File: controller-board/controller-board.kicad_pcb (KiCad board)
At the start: 2 copper layers, 130 x 95 mm, 96 parts, among them J1 Conn_01x02, J2 Conn_01x02, J3 Conn_01x02, J4 Conn_01x02, J5 Conn_01x03, J6 Conn_01x02, J7 Conn_01x02, Q1 PMV45EN2, Q3 RQ3E120ATTB, U1 CAT4201, U2 PocketBeagle, U3 LTC3624, U4 CAT4201, U5 CAT4201, U6 CAT4201, U7 MCP4728, U8 ADC108S022

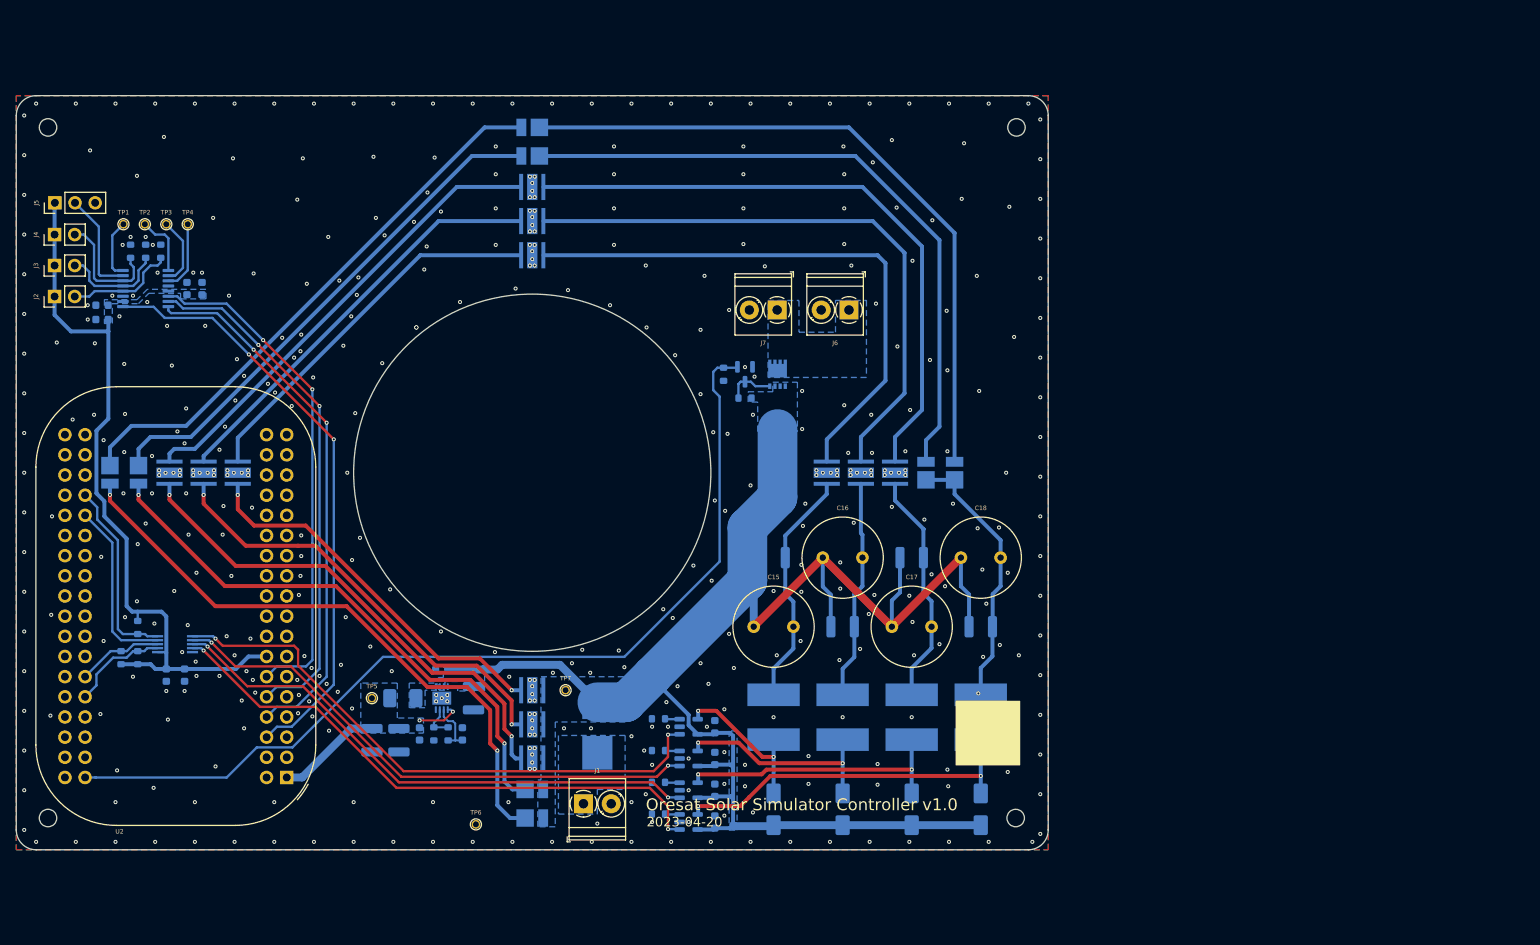
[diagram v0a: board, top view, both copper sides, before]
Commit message: Updated mounting holes and fixed some errors
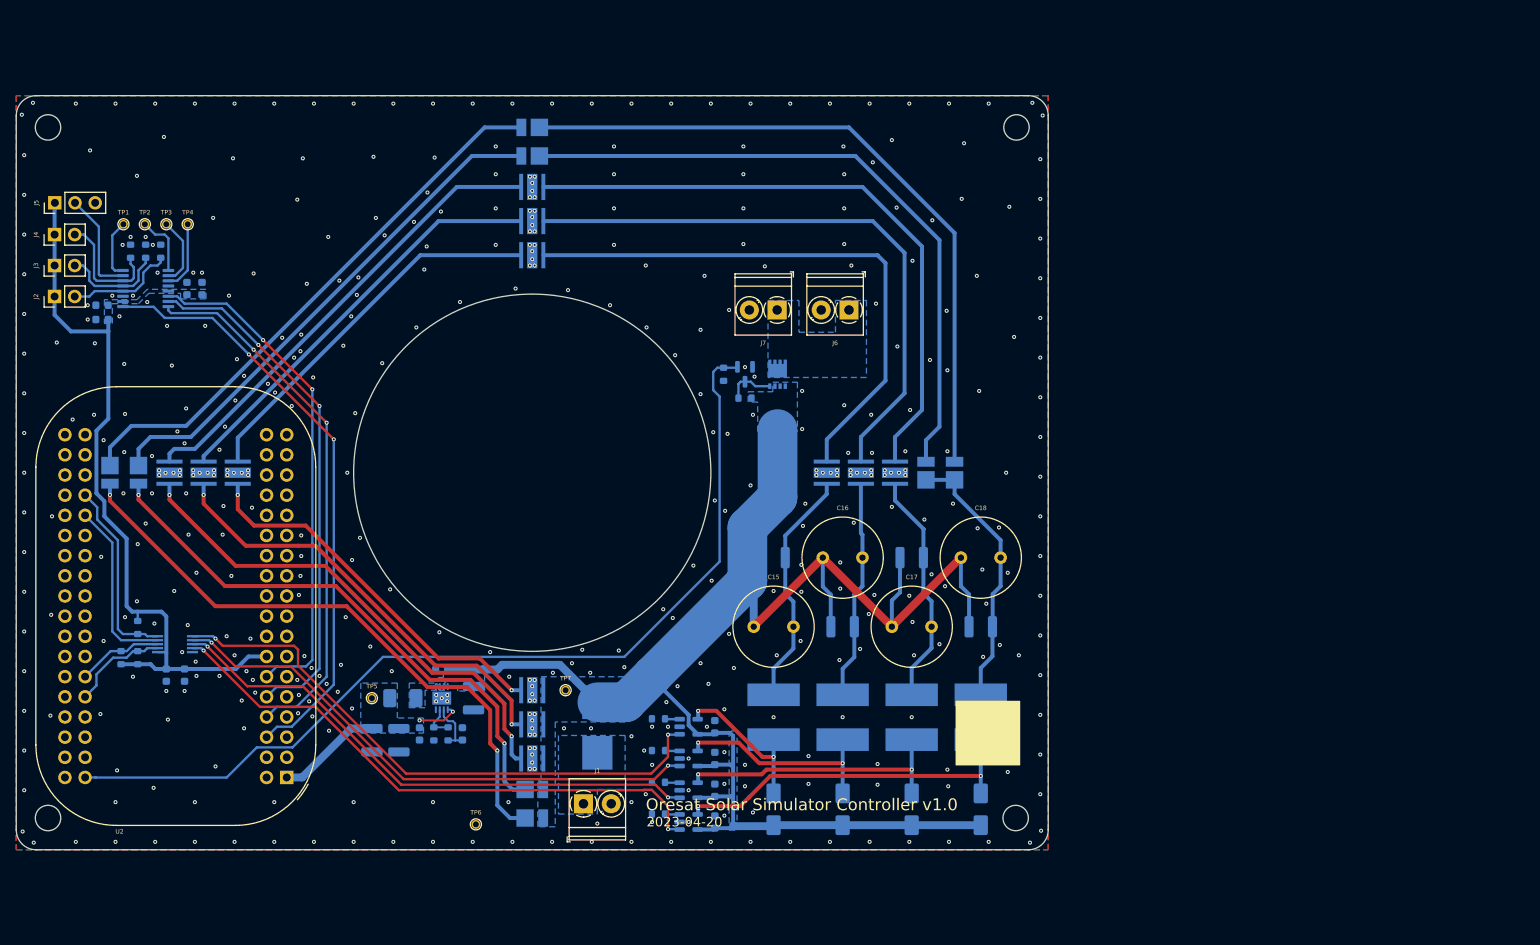
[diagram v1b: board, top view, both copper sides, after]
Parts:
- REF** (x4): value MountingHole_2.2mm_M2 -> MountingHole_3.2mm_M3; footprint MountingHole:MountingHole_2.2mm_M2 -> MountingHole:MountingHole_3.2mm_M3
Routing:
- net GND: vias 454 -> 452

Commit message: Updated main PCB. Added lots of LEDs and moved things around. Fixed some issues.
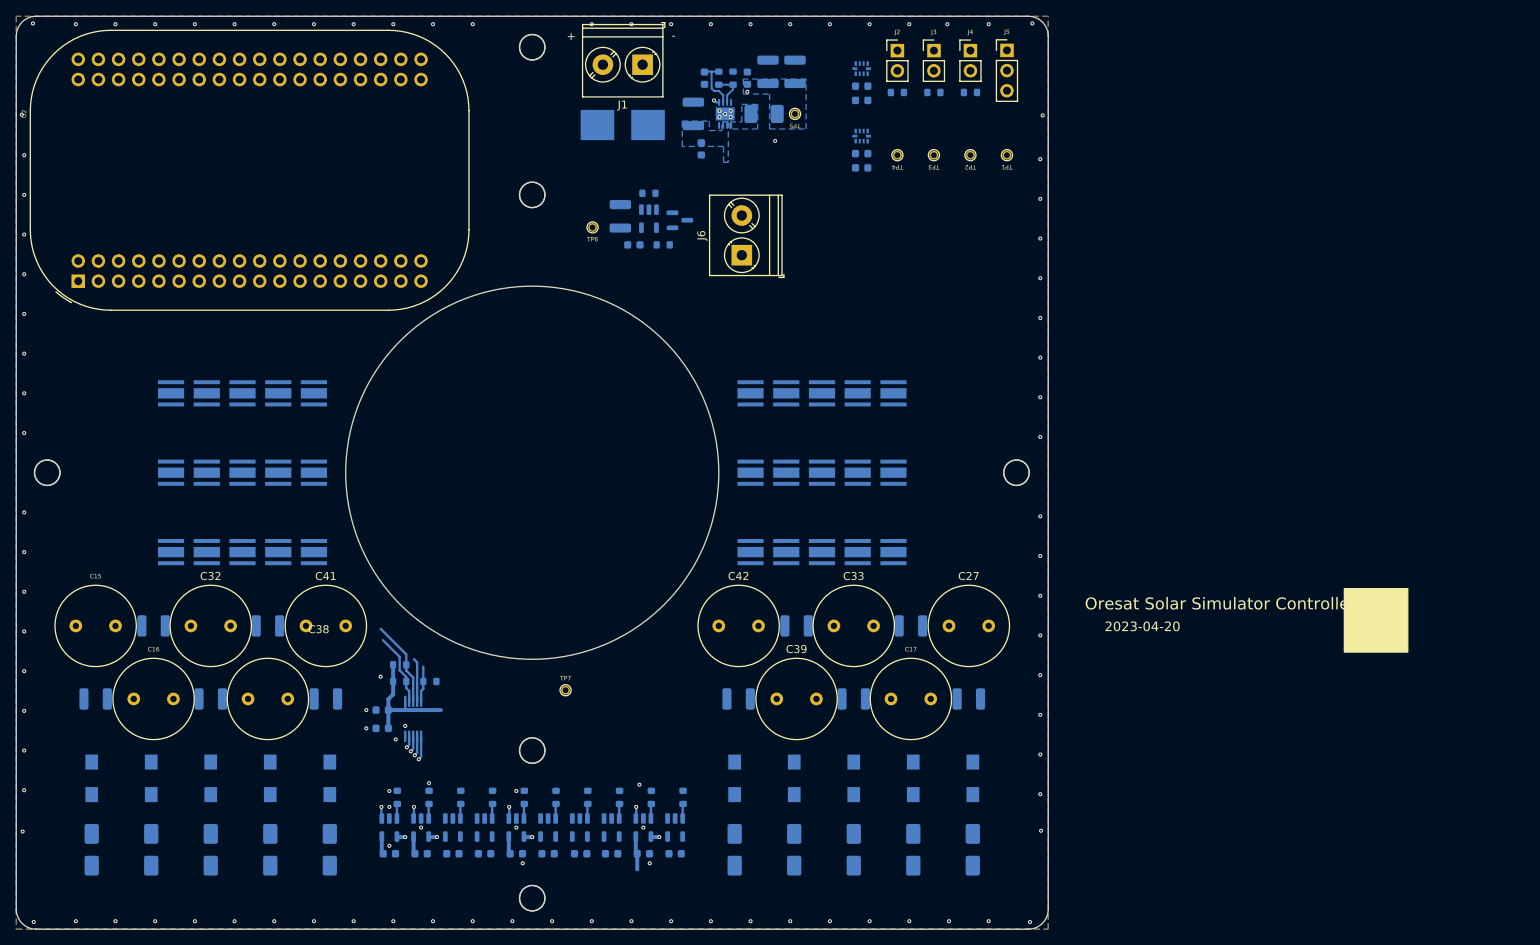
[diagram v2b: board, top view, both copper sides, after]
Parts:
- removed D24: 153283367A212, LED_SMD:LED_PLCC_2835
- removed J7: Conn_01x02, TerminalBlock_Phoenix:TerminalBlock_Phoenix_PT-1,5-2-3.5-H_1x02_P3.50mm_Horizontal
- removed Q3: RQ3E120ATTB, Package_SON:Diodes_PowerDI3333-8
- added C25: 4.7u, Capacitor_SMD:C_0603_1608Metric, B.Cu at (163.0, 150.5)
- added C26: 22u, Capacitor_SMD:C_1210_3225Metric, B.Cu at (200.0, 131.0)
- added C27: NP, Capacitor_THT:C_Radial_D10.0mm_H16.0mm_P5.00mm, F.Cu at (197.5, 121.8)
- added C28: 4.7u, Capacitor_SMD:C_0603_1608Metric, B.Cu at (135.0, 150.5)
- added C29: 4.7u, Capacitor_SMD:C_0603_1608Metric, B.Cu at (155.0, 150.5)
- added C30: 22u, Capacitor_SMD:C_1210_3225Metric, B.Cu at (104.5, 131.0)
- added C31: 22u, Capacitor_SMD:C_1210_3225Metric, B.Cu at (185.5, 131.0)
- added C32: NP, Capacitor_THT:C_Radial_D10.0mm_H16.0mm_P5.00mm, F.Cu at (102.0, 121.8)
- added C33: NP, Capacitor_THT:C_Radial_D10.0mm_H16.0mm_P5.00mm, F.Cu at (183.0, 121.8)
- added C34: 4.7u, Capacitor_SMD:C_0603_1608Metric, B.Cu at (139.0, 150.5)
- added C35: 4.7u, Capacitor_SMD:C_0603_1608Metric, B.Cu at (151.1, 150.5)
- added C36: 22u, Capacitor_SMD:C_1210_3225Metric, B.Cu at (111.7, 121.8)
- added C37: 22u, Capacitor_SMD:C_1210_3225Metric, B.Cu at (178.3, 121.8)
- added C38: NP, Capacitor_THT:C_Radial_D10.0mm_H16.0mm_P5.00mm, F.Cu at (109.2, 131.0)
- added C39: NP, Capacitor_THT:C_Radial_D10.0mm_H16.0mm_P5.00mm, F.Cu at (175.8, 131.0)
- added C40: 22u, Capacitor_SMD:C_1210_3225Metric, B.Cu at (171.0, 131.0)
- added C41: NP, Capacitor_THT:C_Radial_D10.0mm_H16.0mm_P5.00mm, F.Cu at (116.5, 121.8)
- added C42: NP, Capacitor_THT:C_Radial_D10.0mm_H16.0mm_P5.00mm, F.Cu at (168.5, 121.8)
- added C43: 22u, Capacitor_SMD:C_1210_3225Metric, B.Cu at (156.1, 70.2)
- added C44: 1u, Capacitor_SMD:C_0603_1608Metric, B.Cu at (157.8, 73.8)
- added D25: XPEBRD-L1-0000-00501, LED_SMD:LED_Cree-XP, B.Cu at (190.5, 92.5)
- added D26: XPEBRD-L1-0000-00501, LED_SMD:LED_Cree-XP, B.Cu at (190.5, 112.5)
- added D27: XPEBRD-L1-0000-00501, LED_SMD:LED_Cree-XP, B.Cu at (190.5, 102.5)
- added D28: XPEBBL-L1-0000-00201, LED_SMD:LED_Cree-XP, B.Cu at (108.5, 92.5)
- added D29: XPEBBL-L1-0000-00201, LED_SMD:LED_Cree-XP, B.Cu at (108.5, 112.5)
- added D30: XPEBBL-L1-0000-00201, LED_SMD:LED_Cree-XP, B.Cu at (181.5, 92.5)
- added D31: XPEBBL-L1-0000-00201, LED_SMD:LED_Cree-XP, B.Cu at (181.5, 112.5)
- added D32: XPEBBL-L1-0000-00201, LED_SMD:LED_Cree-XP, B.Cu at (108.5, 102.5)
- added D33: XPEBBL-L1-0000-00201, LED_SMD:LED_Cree-XP, B.Cu at (181.5, 102.5)
- added D34: SS210A, Diode_SMD:D_SMA, B.Cu at (112.0, 150.0)
- added D35: SS210A, Diode_SMD:D_SMA, B.Cu at (178.0, 150.0)
- added D36: XPEBBL-L1-0000-00201, LED_SMD:LED_Cree-XP, B.Cu at (113.0, 92.5)
- added D37: XPEBBL-L1-0000-00201, LED_SMD:LED_Cree-XP, B.Cu at (113.0, 112.5)
- added D38: XPEBBL-L1-0000-00201, LED_SMD:LED_Cree-XP, B.Cu at (177.0, 92.5)
- added D39: XPEBBL-L1-0000-00201, LED_SMD:LED_Cree-XP, B.Cu at (177.0, 112.5)
- added D40: XPEBBL-L1-0000-00201, LED_SMD:LED_Cree-XP, B.Cu at (113.0, 102.5)
- added D41: XPEBBL-L1-0000-00201, LED_SMD:LED_Cree-XP, B.Cu at (177.0, 102.5)
- added L10: 56u, Inductor_SMD:L_Wuerth_HCI-5040, B.Cu at (178.0, 141.0)
- added L11: 56u, Inductor_SMD:L_Wuerth_HCI-5040, B.Cu at (170.5, 141.0)
- added L6: 56u, Inductor_SMD:L_Wuerth_HCI-5040, B.Cu at (200.5, 141.0)
- added L7: 56u, Inductor_SMD:L_Wuerth_HCI-5040, B.Cu at (104.5, 141.0)
- added L8: 56u, Inductor_SMD:L_Wuerth_HCI-5040, B.Cu at (185.5, 141.0)
- added L9: 56u, Inductor_SMD:L_Wuerth_HCI-5040, B.Cu at (112.0, 141.0)
- added R14: 10k, Resistor_SMD:R_0603_1608Metric, B.Cu at (164.0, 143.4)
- added R16: 10k, Resistor_SMD:R_0603_1608Metric, B.Cu at (136.0, 143.4)
- added R17: 10k, Resistor_SMD:R_0603_1608Metric, B.Cu at (156.0, 143.4)
- added R18: 10k, Resistor_SMD:R_0603_1608Metric, B.Cu at (140.0, 143.4)
- added R19: 10k, Resistor_SMD:R_0603_1608Metric, B.Cu at (152.0, 143.4)
- added R20: 10k, Resistor_SMD:R_0603_1608Metric, B.Cu at (148.0, 143.4)
- added REF**: MountingHole_3.2mm_M3, MountingHole:MountingHole_3.2mm_M3, F.Cu at (145.0, 156.1)
- added REF**: MountingHole_3.2mm_M3, MountingHole:MountingHole_3.2mm_M3, F.Cu at (145.0, 48.9)
- added U10: CAT4201, Package_TO_SOT_SMD:TSOT-23-5, B.Cu at (163.0, 147.2)
- added U11: CAT4201, Package_TO_SOT_SMD:TSOT-23-5, B.Cu at (135.0, 147.2)
- added U12: CAT4201, Package_TO_SOT_SMD:TSOT-23-5, B.Cu at (155.0, 147.2)
- added U13: CAT4201, Package_TO_SOT_SMD:TSOT-23-5, B.Cu at (139.0, 147.2)
- added U14: CAT4201, Package_TO_SOT_SMD:TSOT-23-5, B.Cu at (151.0, 147.2)
- added U15: CAT4201, Package_TO_SOT_SMD:TSOT-23-5, B.Cu at (147.0, 147.2)
- added U16: DGD0216, Package_TO_SOT_SMD:TSOT-23-5, B.Cu at (159.7, 70.5)
- added U9: ADS1015IRUGR, Package_DFN_QFN:Texas_R-PUQFN-N10, B.Cu at (186.5, 60.1)
- C12, C13: value 4.7u -> 22u; footprint Capacitor_SMD:C_0603_1608Metric -> Capacitor_SMD:C_1210_3225Metric
- C18: value NP -> 22u; footprint Capacitor_THT:C_Radial_D10.0mm_H16.0mm_P5.00mm -> Capacitor_SMD:C_1210_3225Metric; moved to B.Cu
- C2, C3, C4: value 22u -> 4.7u; footprint Capacitor_SMD:C_1210_3225Metric -> Capacitor_SMD:C_0603_1608Metric
- D11, D13, D9: value NP -> XPEBGR-L1-0000-00D01
- D14: value XPEBBL-L1-0000-00201 -> XPEBGR-L1-0000-00D01
- D15, D7: value NP -> SS210A; footprint LED_SMD:LED_Cree-XP -> Diode_SMD:D_SMA
- D16: value XPEBBL-L1-0000-00201 -> SS210A; footprint LED_SMD:LED_Cree-XP -> Diode_SMD:D_SMA
- D17: value 153283367A212 -> SS210A; footprint LED_SMD:LED_PLCC_2835 -> Diode_SMD:D_SMA
- D18, D19, D20, D21, D22, D23: value 153283367A212 -> XPEBBL-L1-0000-00201; footprint LED_SMD:LED_PLCC_2835 -> LED_SMD:LED_Cree-XP
- D5: value NP -> XPEBRD-L1-0000-00501
- J1, J6: footprint TerminalBlock_Phoenix:TerminalBlock_Phoenix_PT-1,5-2-3.5-H_1x02_P3.50mm_Horizontal -> TerminalBlock_Phoenix:TerminalBlock_Phoenix_PT-1,5-2-5.0-H_1x02_P5.00mm_Horizontal
- L1, L2, L3, L4: footprint Inductor_SMD:L_Bourns_SRN8040TA -> Inductor_SMD:L_Wuerth_HCI-5040
- Q1: value PMV45EN2 -> ~
- R10: value 10k -> 0
- R11: value 1k -> 10k
- R5: value 25k -> 10k
- U8: value ADC108S022 -> ADS1015IRUGR; footprint Package_SO:TSSOP-16_4.4x5mm_P0.65mm -> Package_DFN_QFN:Texas_R-PUQFN-N10
- moved J5 121.5 mm to (204.8, 49.3), turned to 0 degrees
- moved J4 117.7 mm to (200.2, 49.3), turned to 0 degrees
- moved J3 114.0 mm to (195.6, 49.3), turned to 0 degrees
- moved TP1 111.6 mm to (204.8, 62.5), turned to 180 degrees
- moved J2 110.6 mm to (191.0, 49.3), turned to 0 degrees
- moved R7 107.7 mm to (200.2, 54.6), turned to 0 degrees
- moved TP2 104.4 mm to (200.2, 62.5), turned to 180 degrees
- moved R6 101.3 mm to (195.6, 54.6), turned to 0 degrees
- moved C8 99.7 mm to (178.1, 52.0), turned to 90 degrees
- moved REF** 99.4 mm to (145.0, 67.5)
- moved C21 98.0 mm to (186.5, 62.3), turned to 0 degrees
- moved C22 97.3 mm to (186.5, 64.1), turned to 0 degrees
- moved TP3 97.1 mm to (195.6, 62.5), turned to 180 degrees
- moved C7 96.2 mm to (174.7, 52.0), turned to 90 degrees
- moved R1 94.9 mm to (191.0, 54.6), turned to 0 degrees
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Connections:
- C12 pad 2: GND -> Net-(D10-K)
- C13 pad 2: GND -> Net-(D12-K)
- C16 pad 2: Net-(D12-K) -> Net-(D10-K)
- C17 pad 2: Net-(D16-K) -> Net-(D12-K)
- C18 pad 2: Net-(D23-K) -> Net-(D19-K)
- C2 pad 2: Net-(D12-K) -> GND
- C3 pad 2: Net-(D16-K) -> GND
- C4 pad 2: Net-(D23-K) -> GND
- D11 pad 2: Net-(D10-K) -> VCC
- D12 pad 2: Net-(D11-K) -> Net-(D12-A)
- D13 pad 1: Net-(D13-K) -> Net-(D10-A)
- D13 pad 2: VCC -> Net-(D13-A)
- D14 pad 1: Net-(D14-K) -> Net-(D12-A)
- D14 pad 2: Net-(D13-K) -> Net-(D11-K)
- D15 pad 1: Net-(D15-K) -> VCC
- D15 pad 2: Net-(D14-K) -> Net-(D15-A)
- D16 pad 1: Net-(D16-K) -> VCC
- D16 pad 2: Net-(D15-K) -> Net-(D16-A)
- D17 pad 1: Net-(D17-K) -> VCC
- D17 pad 2: VCC -> Net-(D17-A)
- D19 pad 2: Net-(D17-K) -> Net-(D19-A)
- D20 pad 2: Net-(D18-K) -> VCC
- D21 pad 2: Net-(D19-K) -> Net-(D21-A)
- D22 pad 1: Net-(D22-K) -> Net-(D19-A)
- D22 pad 2: Net-(D20-K) -> Net-(D18-K)
- D23 pad 1: Net-(D23-K) -> Net-(D21-A)
- D23 pad 2: Net-(D21-K) -> Net-(D20-K)
- D7 pad 1: Net-(D7-K) -> VCC
- D7 pad 2: Net-(D6-K) -> Net-(D7-A)
- D8 pad 2: Net-(D7-K) -> Net-(D6-K)
- D9 pad 1: Net-(D10-A) -> Net-(D13-A)
- F1 pad 1: Net-(J1-Pin_1) -> Net-(J1-Pin_2)
- J1 pad 1: Net-(J1-Pin_1) -> GND
- J1 pad 2: GND -> Net-(J1-Pin_2)
- J6 pad 2: GND -> VCC
- L2 pad 2: Net-(D12-K) -> Net-(D10-K)
- L3 pad 2: Net-(D16-K) -> Net-(D12-K)
- L4 pad 2: Net-(D23-K) -> Net-(D19-K)
- Q1 pad 3: Net-(Q1-D) -> Net-(J6-Pin_1)
- R10 pad 1: Net-(Q1-G) -> Net-(U16-OUT)
- R10 pad 2: GND -> Net-(Q1-G)
- R11 pad 1: VCC -> Net-(U16-IN)
- R11 pad 2: Net-(Q1-D) -> GND
- TP1 pad 1: Net-(U8-IN4) -> Net-(U9-AIN0)
- TP2 pad 1: Net-(U8-IN5) -> Net-(U9-AIN1)
- TP3 pad 1: Net-(U8-IN6) -> Net-(U9-AIN2)
- TP4 pad 1: Net-(U8-IN7) -> Net-(U9-AIN3)
- U2 pad 10: Net-(U2-SPI0.MISO) -> unconnected-(U2-SPI0.MISO-Pad10)
- U2 pad 12: Net-(U2-SPI0.MOSI) -> unconnected-(U2-SPI0.MOSI-Pad12)
- U2 pad 37: Net-(Q1-G) -> Net-(U16-IN)
- U2 pad 6: Net-(U2-SPI0.CS) -> unconnected-(U2-SPI0.CS-Pad6)
- U2 pad 8: Net-(U2-SPI0.CLK) -> unconnected-(U2-SPI0.CLK-Pad8)
- U5 pad 1: /BLUE_LIM -> /GREEN_LIM
- U8 pad 1: Net-(U2-SPI0.CS) -> GND
- U8 pad 10: Net-(U8-IN6) -> /SCL1
- U8 pad 2: +3.3V -> unconnected-(U8-ALERT/RDY-Pad2)
- U8 pad 8: Net-(U8-IN4) -> +3.3V
- U8 pad 9: Net-(U8-IN5) -> /SDA1
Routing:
- net VCC: track 208.4 -> 10.2 mm
- net Net-(Q1-G): track 118.7 -> 0.00 mm
- net Net-(D22-K): track 86.6 -> 0.00 mm
- net Net-(D21-K): track 83.4 -> 0.00 mm
- net Net-(D15-K): track 79.3 -> 0.00 mm
- net +3.3V: track 93.8 -> 16.0 mm
- net Net-(D18-K): track 77.5 -> 0.00 mm, vias 2 -> 0
- net Net-(D11-K): track 75.7 -> 0.00 mm
- net Net-(U2-SPI0.CS): track 75.6 -> 0.00 mm, vias 2 -> 0
- net Net-(D7-K): track 71.6 -> 0.00 mm
- net Net-(D17-K): track 70.8 -> 0.00 mm, vias 2 -> 0
- net Net-(D20-K): track 70.8 -> 0.00 mm
- net /UV_LIM: track 72.6 -> 3.01 mm
- net /RED_LIM: track 73.4 -> 4.51 mm
- net Net-(U2-SPI0.CLK): track 68.0 -> 0.00 mm, vias 2 -> 0
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- removed copper zone on B.Cu, net +3.3V
- removed copper zone on B.Cu, net Net-(J1-Pin_1)
- removed copper zone on B.Cu, net Net-(J6-Pin_1)
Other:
- board size 130 x 95 mm -> 130 x 115 mm
